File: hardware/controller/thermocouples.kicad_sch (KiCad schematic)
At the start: 12 parts, among them J1 Conn_01x02_Pin, J2 Conn_01x02_Pin, J3 Conn_01x02_Pin, J4 Conn_01x02_Pin, U2 MAX31855KASA, U3 MAX31855KASA, U4 MAX31855KASA, U5 MAX31855KASA

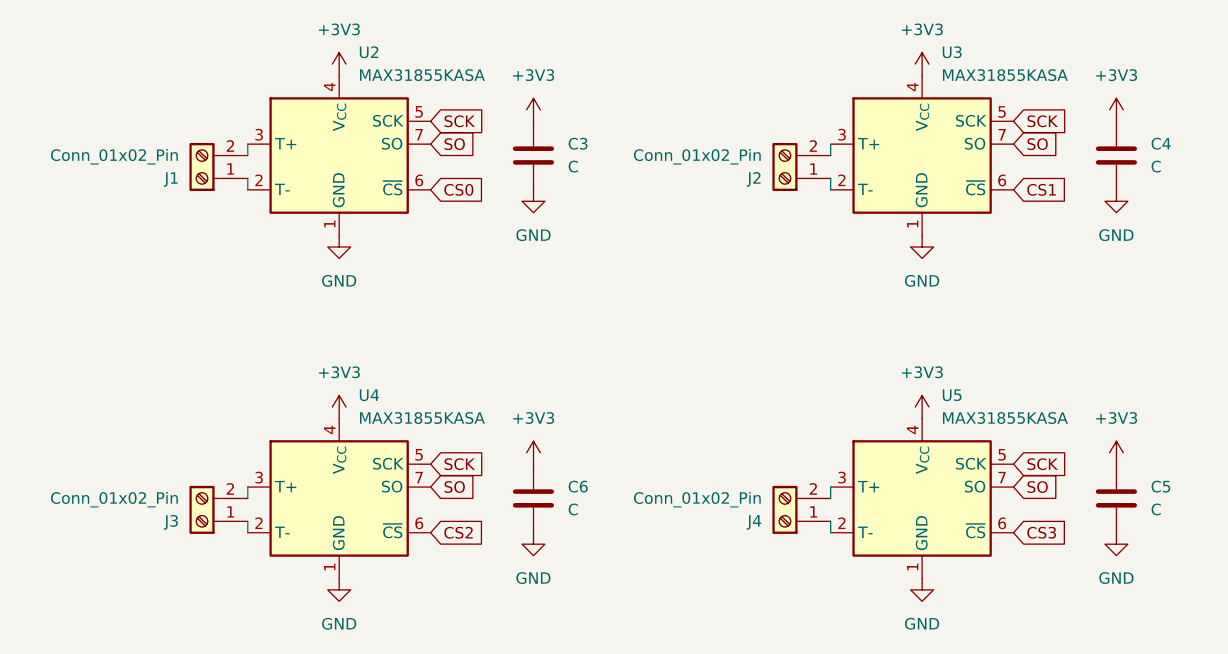
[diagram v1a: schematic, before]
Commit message: Filled out power section of schematic
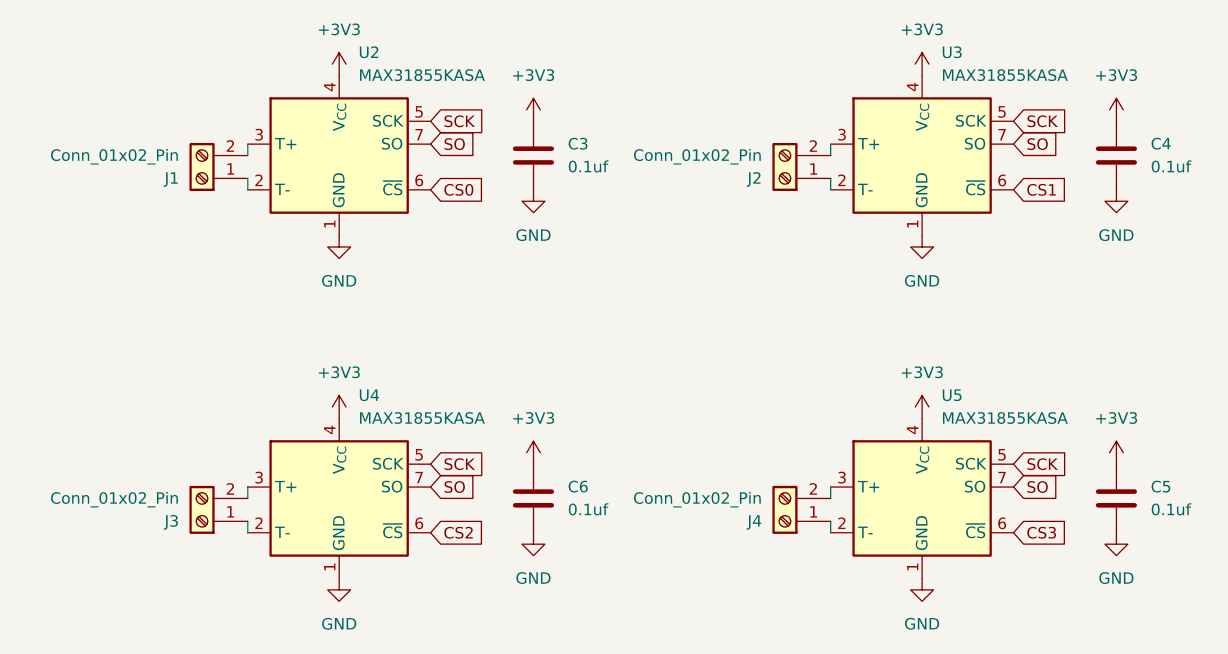
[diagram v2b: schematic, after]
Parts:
- C3, C4, C5, C6: value C -> 0.1uf
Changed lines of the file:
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@@
 			)
 		)
-		(property "Value" "C"
+		(property "Value" "0.1uf"
 			(at 129.54 109.2199 0)
 			(effects
@@
 			)
 		)
-		(property "Value" "C"
+		(property "Value" "0.1uf"
 			(at 194.31 109.2199 0)
 			(effects
@@
 			)
 		)
-		(property "Value" "C"
+		(property "Value" "0.1uf"
 			(at 129.54 71.1199 0)
 			(effects
@@
 			)
 		)
-		(property "Value" "C"
+		(property "Value" "0.1uf"
 			(at 194.31 71.1199 0)
 			(effects

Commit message: Fix USB symbol, adjust decoupling caps
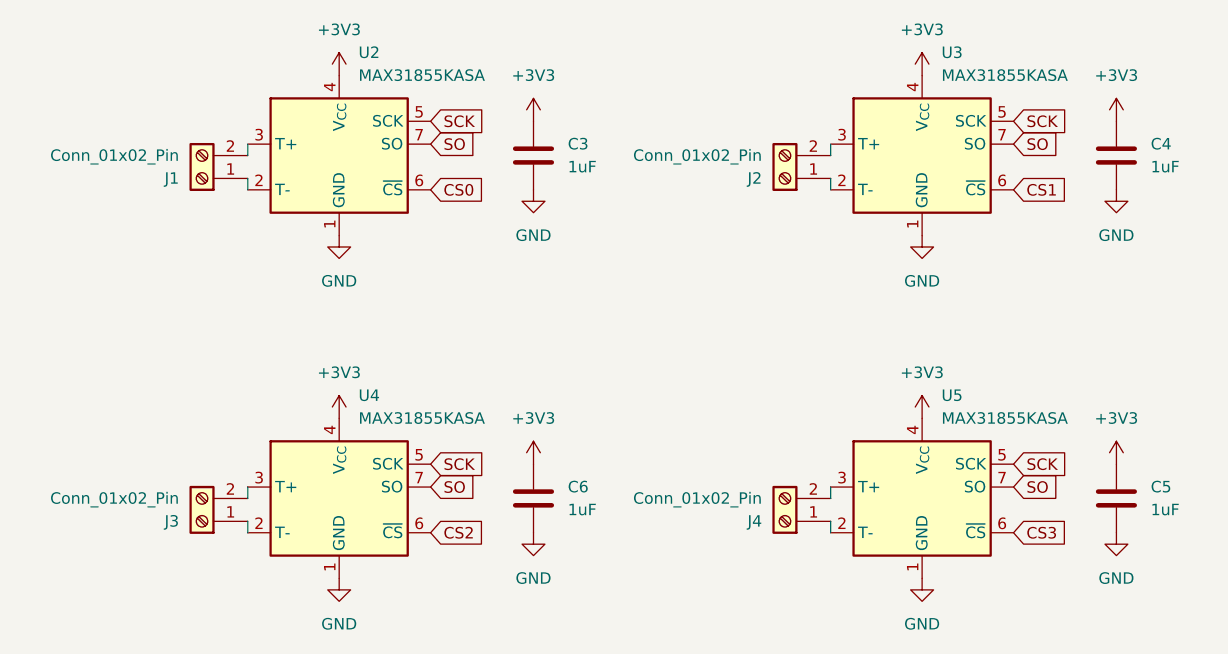
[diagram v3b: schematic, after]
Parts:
- C3, C4, C5, C6: value 0.1uf -> 1uF
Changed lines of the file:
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@@
 			)
 		)
-		(property "Value" "0.1uf"
+		(property "Value" "1uF"
 			(at 129.54 109.2199 0)
 			(effects
@@
 			)
 		)
-		(property "Value" "0.1uf"
+		(property "Value" "1uF"
 			(at 194.31 109.2199 0)
 			(effects
@@
 			)
 		)
-		(property "Value" "0.1uf"
+		(property "Value" "1uF"
 			(at 129.54 71.1199 0)
 			(effects
@@
 			)
 		)
-		(property "Value" "0.1uf"
+		(property "Value" "1uF"
 			(at 194.31 71.1199 0)
 			(effects

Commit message: Drop to 3x thermocouples, 2x fans
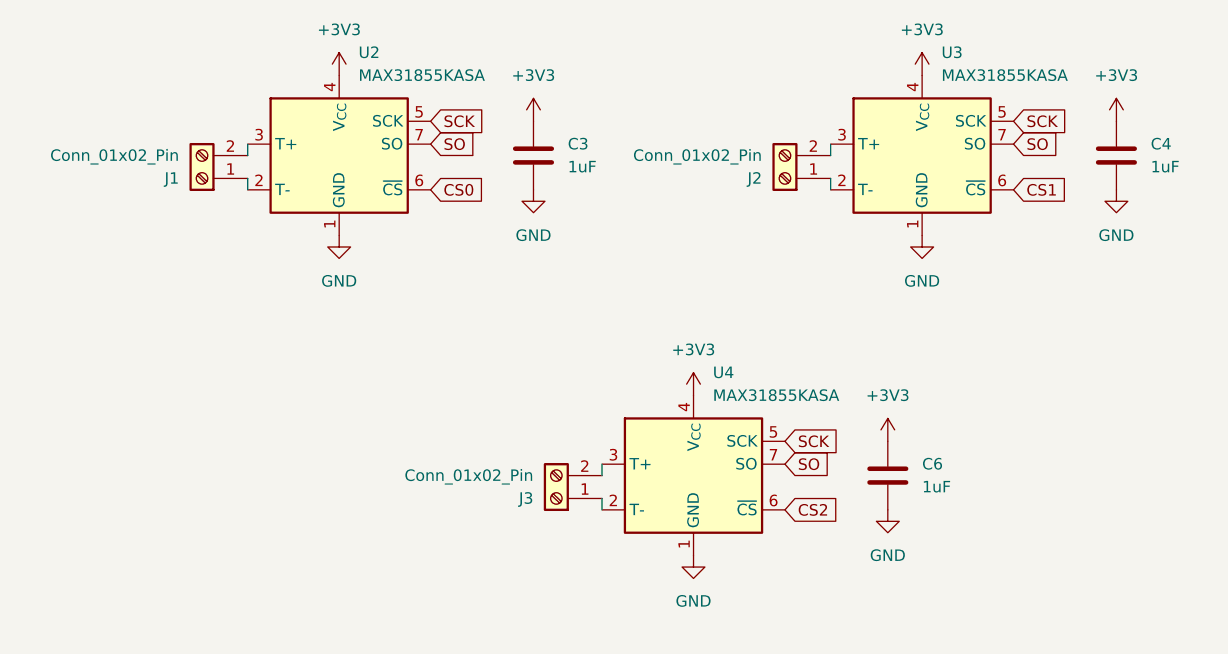
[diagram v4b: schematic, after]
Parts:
- removed C5: 1uF, Capacitor_SMD:C_0805_2012Metric, symbol Device:C
- removed J4: Conn_01x02_Pin, TerminalBlock_4Ucon:TerminalBlock_4Ucon_1x02_P3.50mm_Horizontal, symbol Connector:Screw_Terminal_01x02
- removed U5: MAX31855KASA, Package_SO:SOIC-8_3.9x4.9mm_P1.27mm, symbol Sensor_Temperature:MAX31855KASA
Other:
- moved on the sheet: C6, J3, U4

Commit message: Add LCSC numbers
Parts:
- C3, C4, C6: LCSC (none) -> C28323
- U2, U3, U4: LCSC (none) -> C52028
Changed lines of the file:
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@@
+			)
+		)
+		(property "LCSC" "C52028"
+			(at 143.51 106.68 0)
+			(effects
+				(font
+					(size 1.27 1.27)
+				)
+				(hide yes)
 			)
 		)
@@
 			)
 		)
+		(property "LCSC" "C28323"
+			(at 165.1 105.41 0)
+			(effects
+				(font
+					(size 1.27 1.27)
+				)
+				(hide yes)
+			)
+		)
 		(pin "1"
 		)
@@
 			)
 		)
+		(property "LCSC" "C52028"
+			(at 104.14 71.12 0)
+			(effects
+				(font
+					(size 1.27 1.27)
+				)
+				(hide yes)
+			)
+		)
 		(pin "5"
 		)
@@
 			)
 		)
+		(property "LCSC" "C28323"
+			(at 125.73 69.85 0)
+			(effects
+				(font
+					(size 1.27 1.27)
+				)
+				(hide yes)
+			)
+		)
 		(pin "1"
 		)
@@
 			)
 		)
+		(property "LCSC" "C52028"
+			(at 168.91 71.12 0)
+			(effects
+				(font
+					(size 1.27 1.27)
+				)
+				(hide yes)
+			)
+		)
 		(pin "8"
 		)
@@
 			(at 190.5 69.85 0)
 			(effects
+				(font
+					(size 1.27 1.27)
+				)
+				(hide yes)
+			)
+		)
+		(property "LCSC" "C28323"
+			(at 190.5 69.85 0)
+			(effects
